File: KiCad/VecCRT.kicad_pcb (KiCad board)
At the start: 2 copper layers, 90 x 70 mm, 75 parts, among them J1 RaspiGPIO, J2 K2, J3 Conn_01x03, J4 Conn_01x06, J5 Conn_01x03, J6 Conn_01x06, J7 K2, Q1 2N7000, Q10 2N7000, Q2 2N7002, Q3 2N7002, Q4 2N7000, Q9 2N7000, U1 MCP4822, U2 4066, U3 4066, U4 TL072, U5 TL072, U6 4011, U7 40106, U8 4011

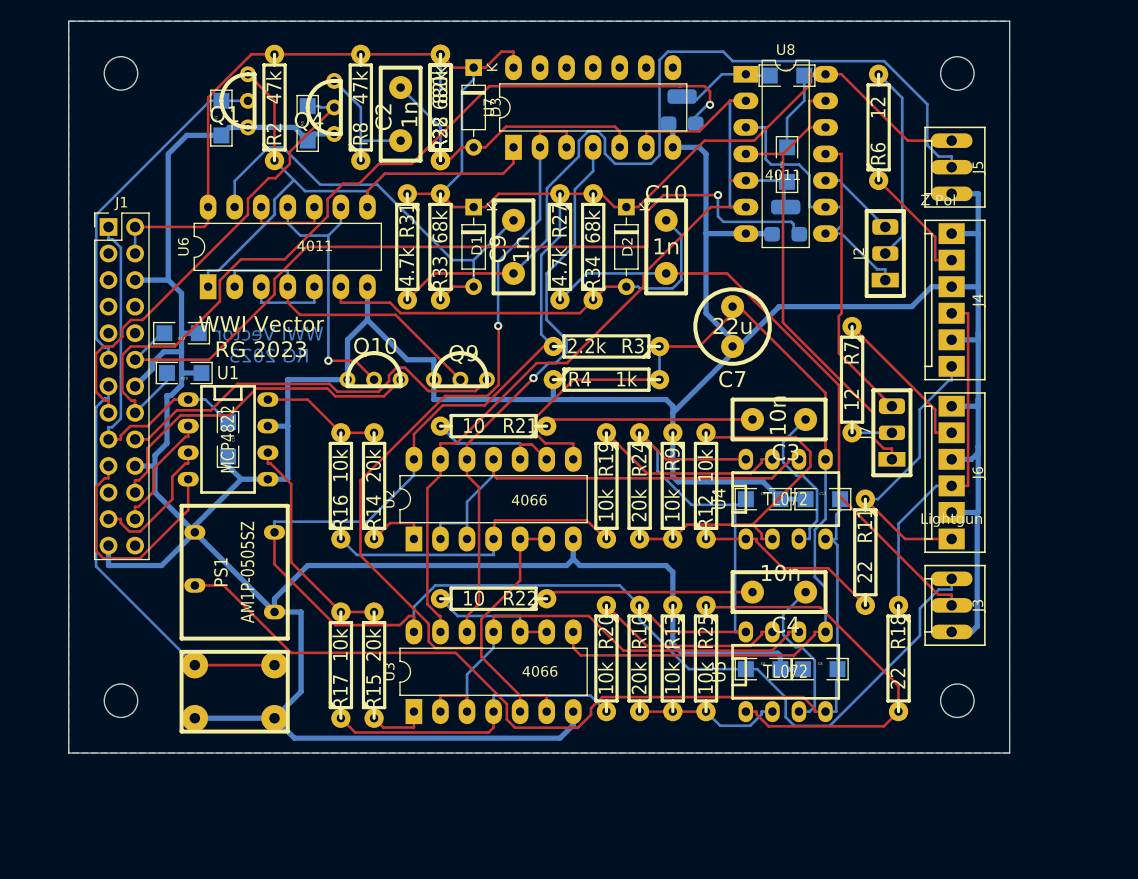
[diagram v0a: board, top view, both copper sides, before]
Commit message: new one-shot light-gun
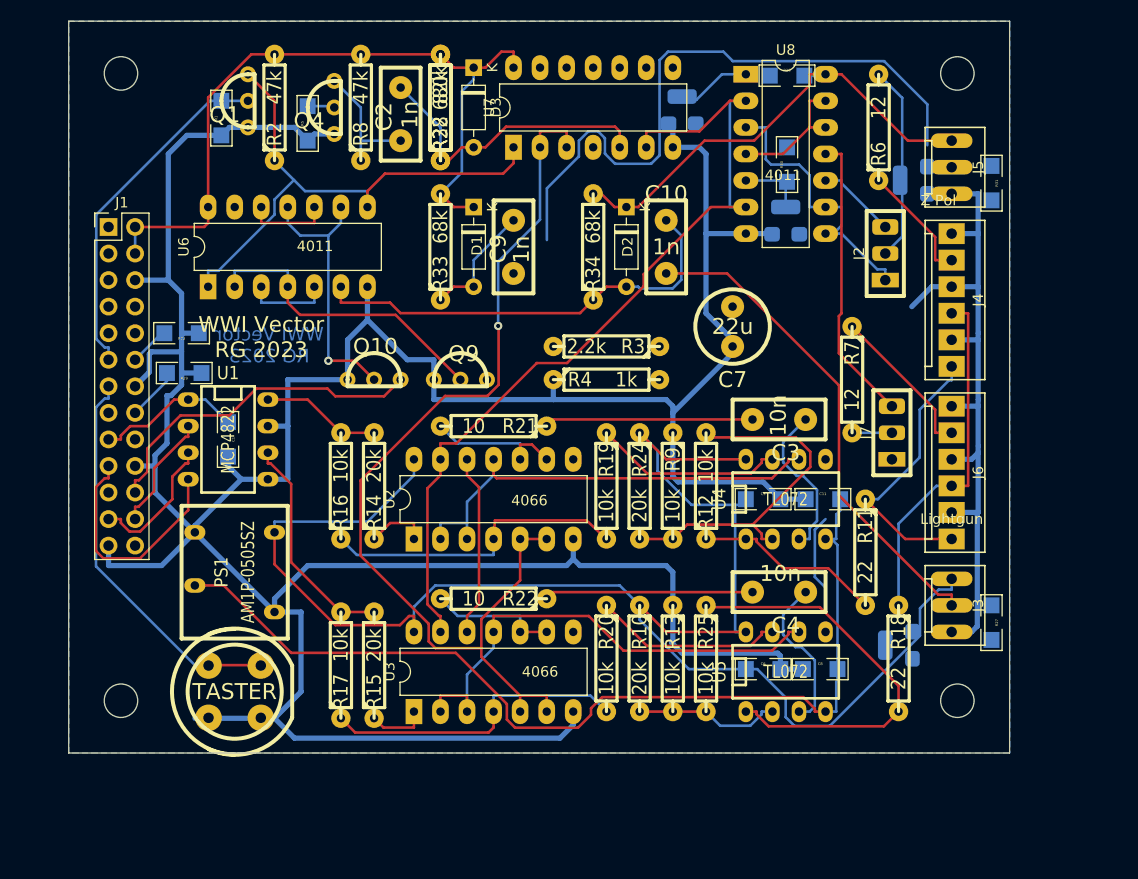
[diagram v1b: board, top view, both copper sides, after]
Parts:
- added Q5: 2N7002, RG:SOT-23_GDS, B.Cu at (80.8, 15.2)
- added Q6: 2N7002, RG:SOT-23_GDS, B.Cu at (79.4, 59.7)
- R27, R31: value 4.7k -> 470k; footprint RG:R4-2 -> RG:SM-1206B
- S1: footprint RG:Tast2mil -> RG:Tast-DT6
- moved R31 56.2 mm to (88.3, 15.5)
- moved R27 54.7 mm to (88.3, 57.5)
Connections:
- C10 pad 1: Net-(C10-Pad1) -> Net-(R27-Pad1)
- J1 pad 26: unconnected-(J1-Pad26) -> /isGun2on
- J1 pad 7: unconnected-(J1-Pad7) -> /isGun1on
- J1 pad 9: unconnected-(J1-Pad9) -> GND
- J3 pad 2: Net-(C10-Pad1) -> Net-(R27-Pad1)
- R27 pad 1: +5V -> Net-(R27-Pad1)
- R27 pad 2: Net-(C10-Pad1) -> GND
- R31 pad 1: +5V -> Net-(C9-Pad1)
- R31 pad 2: Net-(C9-Pad1) -> GND
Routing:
- net GND: track 601.6 -> 487.9 mm, vias 2 -> 0
- net /mid: track 95.4 -> 0.00 mm
- net Net-(C9-Pad1): track 81.9 -> 0.00 mm
- net +5V: track 337.7 -> 276.6 mm
- net Net-(C10-Pad1): track 58.4 -> 0.00 mm
- net Net-(R27-Pad1): track 0.00 -> 47.2 mm
- net /doDRAW: track 43.5 -> 2.59 mm
- net /isGUN2: track 38.8 -> 0.00 mm
- net /~{move}: track 54.4 -> 17.5 mm, vias 1 -> 0
- net Net-(J7-Pad3): track 46.7 -> 12.7 mm
- net Net-(C9-Pad2): track 42.8 -> 11.6 mm
- net /V_ADC: track 35.8 -> 14.1 mm
- net /~{enZ2}: track 0.00 -> 5.07 mm
- net /~{enZ1}: track 0.00 -> 3.85 mm
- net /enZ1: track 9.43 -> 7.10 mm
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
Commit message: KiCad: EDA updates for PCB production; preliminary tap and switches; ReadMe.md updated
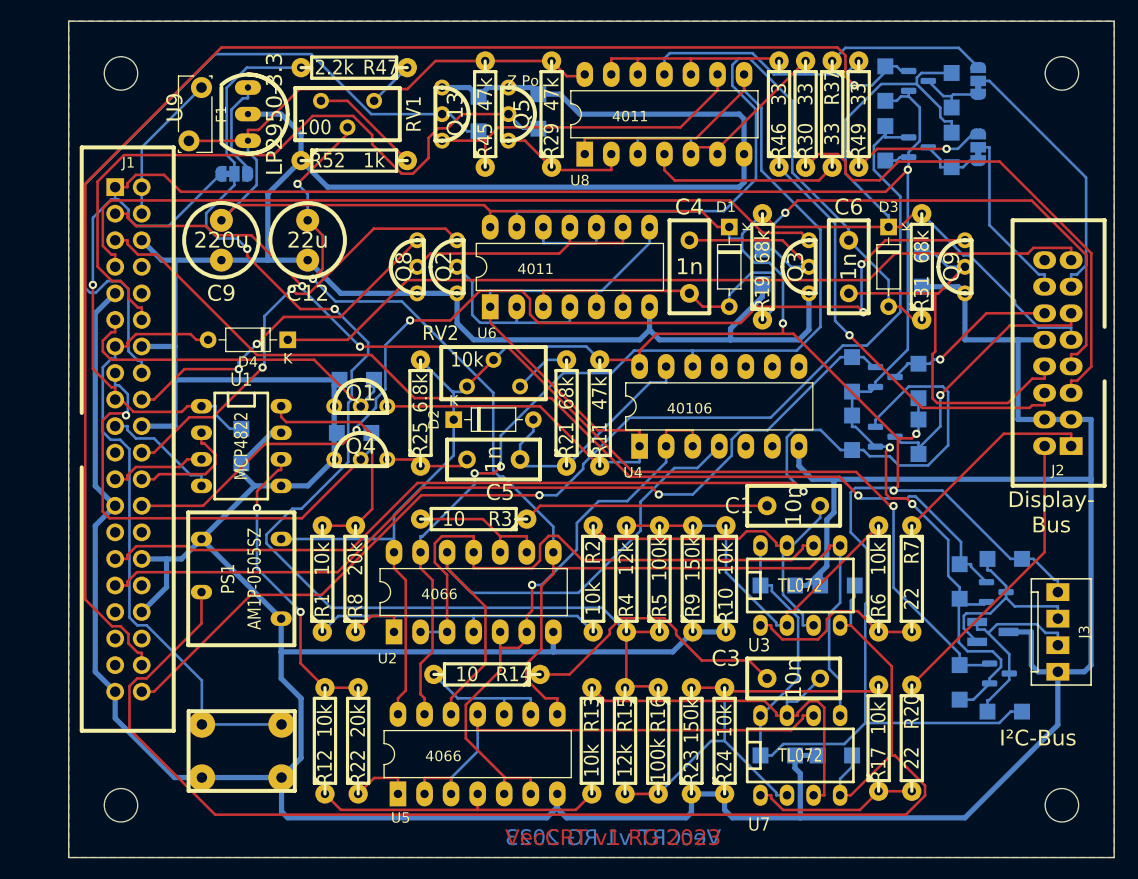
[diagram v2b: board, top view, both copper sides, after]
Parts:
- removed the C4 at (67.9, 54.6)
- removed the D1 at (38.7, 17.8)
- removed J4, J6: Conn_01x06, RG:PSS_6
- removed J5: Conn_01x03, RG:PSS_3
- removed J7: K2, RG:Pins_3
- removed the Q2 at (58.7, 8.51)
- removed the Q3 at (68.6, 19.1)
- removed the R1 at (14.6, 9.27)
- removed the R10 at (54.6, 61.0)
- removed the R2 at (19.7, 8.26)
- removed the R25 at (61.0, 61.0)
- removed R26: 47k, RG:SM-1206B
- removed the R28 at (35.6, 8.26)
- removed the R6 at (77.5, 10.2)
- removed the R7 at (74.9, 34.3)
- removed the U3 at (33.0, 66.0)
- added C3: 10n, RG:C2-2, F.Cu at (69.3, 62.9)
- added C6: 1n, RG:C2-2, F.Cu at (74.6, 23.5)
- added D3: 1N914, Diode_THT:D_DO-35_SOD27_P7.62mm_Horizontal, F.Cu at (78.4, 19.7)
- added D4: BAT41, Diode_THT:D_DO-35_SOD27_P7.62mm_Horizontal, F.Cu at (21.0, 30.5)
- added D5: ESDA5V3, Package_TO_SOT_SMD:SOT-23_Handsoldering, B.Cu at (88.4, 58.4)
- added F1: Polyfuse, Fuse:Fuse_Bourns_MF-RG300, F.Cu at (12.7, 6.35)
- added JP1: SolderJumper_3_Open, Jumper:SolderJumper-3_P1.3mm_Bridged12_RoundedPad1.0x1.5mm, B.Cu at (87.0, 5.71)
- added JP2: SolderJumper_3_Open, Jumper:SolderJumper-3_P1.3mm_Bridged12_RoundedPad1.0x1.5mm, B.Cu at (87.0, 12.1)
- added JP3: SolderJumper_3_Bridged12, Jumper:SolderJumper-3_P1.3mm_Bridged12_RoundedPad1.0x1.5mm, B.Cu at (15.8, 14.6)
- added Q11: BSS138, Package_TO_SOT_SMD:SOT-23, B.Cu at (81.3, 12.1)
- added Q12: BSS138, Package_TO_SOT_SMD:SOT-23, B.Cu at (88.7, 54.6)
- added Q13: 2N7000, RG:FETsgd_inline, F.Cu at (35.7, 8.89)
- added Q14: BSS138, Package_TO_SOT_SMD:SOT-23, B.Cu at (89.0, 62.4)
- added Q6: BSS138, Package_TO_SOT_SMD:SOT-23, B.Cu at (78.1, 39.8)
- added Q7: BSS138, Package_TO_SOT_SMD:SOT-23, B.Cu at (81.3, 5.71)
- added Q8: 2N7000, RG:FETsgd_inline, F.Cu at (33.3, 23.5)
- added Q9: 2N7000, RG:FETsgd_inline, F.Cu at (85.7, 23.5)
- added R11: 47k, RG:R4-2, F.Cu at (50.8, 37.5)
- added R12: 10k, RG:R4-2, F.Cu at (24.5, 68.8)
- added R14: 10, RG:R4-2, F.Cu at (40.0, 62.5)
- added R16: 100k, RG:R4-2, F.Cu at (56.4, 68.8)
- added R24: 10k, RG:R4-2, F.Cu at (62.7, 68.8)
- added R32: 6.8k, RG:SM-1206B, F.Cu at (74.9, 39.4)
- added R34: 6.8k, RG:SM-1206B, F.Cu at (78.1, 5.97)
- added R35: 12k, RG:SM-1206B, F.Cu at (84.5, 6.60)
- added R36: 47k, RG:SM-1206B, F.Cu at (44.9, 8.64)
- added R37: 33, RG:R4-2, F.Cu at (73.0, 8.89)
- added R38: 6.8k, RG:SM-1206B, F.Cu at (74.9, 33.8)
- added R39: 12k, RG:SM-1206B, F.Cu at (81.3, 34.4)
- added R40: 6.8k, RG:SM-1206B, F.Cu at (78.1, 11.7)
- added R41: 12k, RG:SM-1206B, F.Cu at (84.5, 12.3)
- added R42: 470k, RG:SM-1206B, F.Cu at (81.6, 23.7)
- added R43: 6.8k, RG:SM-1206B, F.Cu at (85.2, 53.6)
- added R44: 12k, RG:SM-1206B, F.Cu at (89.5, 51.4)
- added R45: 47k, RG:R4-2, F.Cu at (39.8, 8.89)
- added R46: 33, RG:R4-2, F.Cu at (67.9, 8.89)
- added R48: 47k, RG:SM-1206B, F.Cu at (39.2, 8.89)
- added R49: 33, RG:R4-2, F.Cu at (75.6, 8.89)
- added R5: 100k, RG:R4-2, F.Cu at (56.5, 53.3)
- added R50: 6.8k, RG:SM-1206B, F.Cu at (85.2, 63.2)
- added R51: 12k, RG:SM-1206B, F.Cu at (89.5, 66.0)
- added R9: 150k, RG:R4-2, F.Cu at (59.7, 53.3)
- added RV1: 100, RG:Pot64y, F.Cu at (26.7, 8.89)
- added RV2: 10k, RG:Pot64y, F.Cu at (40.6, 33.7)
- added U7: TL072, RG:DIP-8_300, F.Cu at (70.0, 70.2)
- added U9: LP2950-3.3, RG:TO-92ViGNDVo, F.Cu at (17.1, 8.89)
- C9: value 1n -> 220u; footprint RG:C2-2 -> RG:C2-7
- J1: value RaspiGPIO -> RaspiGPIO40; footprint Connector_PinHeader_2.54mm:PinHeader_2x13_P2.54mm_Vertical -> RG:Wannenstecker_2x20_V
- J2: value K2 -> Conn_02x08_Odd_Even; footprint RG:Pins_3 -> RG:Wannenstecker_2x08_V
- J3: value Conn_01x03 -> Conn_01x04_Female; footprint RG:PSS_3 -> RG:PSS_4
- Q10: value 2N7000 -> BSS138; footprint RG:FETsgd_inline -> Package_TO_SOT_SMD:SOT-23; moved to B.Cu
- Q3: renamed from Q6; value 2N7002 -> 2N7000; footprint RG:SOT-23_GDS -> RG:FETsgd_inline; moved to F.Cu
- Q5: value 2N7002 -> 2N7000; footprint RG:SOT-23_GDS -> RG:FETsgd_inline; moved to F.Cu
- R15: value 20k -> 12k
- R18: value 22 -> 47k; footprint RG:R4-2 -> RG:SM-1206B
- R20: value 10k -> 22
- R21: renamed from R32; value 680k -> 68k
- R22: value 10 -> 20k
- R23: value 47k -> 150k; footprint RG:SM-1206B -> RG:R4-2
- R25: renamed from R8; value 47k -> 6.8k
- R29: footprint RG:SM-1206B -> RG:R4-2
- R30: value 47k -> 33; footprint RG:SM-1206B -> RG:R4-2
- R31: value 470k -> 68k; footprint RG:SM-1206B -> RG:R4-2
- R33: value 68k -> 12k; footprint RG:R4-2 -> RG:SM-1206B
- R4: renamed from R24; value 20k -> 12k
- S1: footprint RG:Tast-DT6 -> RG:Tast2mil
- U4: renamed from U7; footprint Package_DIP:DIP-14_W7.62mm_LongPads -> RG:DIP-14_W7.62mm_LongPads
- U5: value TL072 -> 4066; footprint RG:DIP-8_300 -> RG:DIP-14_W7.62mm_LongPads
- moved R23 62.4 mm to (59.6, 68.8), turned to 90 degrees
- moved R18 58.3 mm to (27.6, 34.3), turned to 0 degrees
- moved R17 51.9 mm to (77.5, 68.6)
- moved R33 49.2 mm to (81.3, 39.8)
- moved Q10 48.9 mm to (78.1, 34.0), turned to 0 degrees
- moved R29 43.0 mm to (46.2, 8.89), turned to 90 degrees
- moved C12 41.5 mm to (22.9, 21.0)
- moved R27 40.5 mm to (66.4, 23.5)
- moved Q5 39.3 mm to (42.1, 8.89), turned to 0 degrees
- moved U5 38.9 mm to (31.5, 73.9), turned to 90 degrees
- moved Q3 37.2 mm to (70.8, 23.5), turned to 180 degrees
- moved R47 36.0 mm to (27.3, 4.45)
- moved C5 34.2 mm to (40.6, 41.9), turned to 0 degrees
- moved Q4 33.8 mm to (27.9, 41.9), turned to 90 degrees
- moved D2 33.7 mm to (36.8, 38.1), turned to 0 degrees
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- renumbered C3 to C1, C8 to C10, C7 to C12, C1 to C2, C10 to C4, C2 to C5, C5 to C7, C6 to C8, D2 to D1, D3 to D2, Q9 to Q2, R16 to R1, R9 to R10, R34 to R19, R19 to R2, R5 to R28, R21 to R3, R3 to R47, R4 to R52, R12 to R6, R11 to R7, R14 to R8, U4 to U3
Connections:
- C2 pad 1: /V_ADC -> +3.3V
- C4 pad 1: Net-(R27-Pad1) -> /gun1
- C5 pad 2: Net-(C2-Pad2) -> Net-(C5-Pad2)
- C9 pad 1: Net-(C9-Pad1) -> +5V
- C9 pad 2: Net-(C9-Pad2) -> GND
- D2 pad 2: Net-(C2-Pad2) -> Net-(C5-Pad2)
- J1 pad 1: /Vref_3.3V -> +3.3V
- J1 pad 13: /isKEY -> /isButton
- J1 pad 17: /V_ADC -> +3.3V
- J1 pad 2: +5V -> Net-(F1-Pad1)
- J1 pad 3: unconnected-(J1-Pad3) -> /SDA_3
- J1 pad 4: +5V -> Net-(F1-Pad1)
- J1 pad 5: unconnected-(J1-Pad5) -> /SCL_3
- J2 pad 1: Net-(J2-Pad1) -> /Xout
- J2 pad 2: Net-(J2-Pad2) -> /Yout
- J2 pad 3: Net-(J2-Pad3) -> GND
- J3 pad 2: Net-(R27-Pad1) -> Net-(D5-Pad1)
- J3 pad 3: GND -> Net-(D5-Pad2)
- Q2 pad D: /isGUN2 -> /isGUN1
- Q3 pad D: /isGun2on -> /isGun1on
- Q3 pad G: Net-(R27-Pad1) -> /gun1
- Q5 pad D: /isGun1on -> Net-(Q5-PadD)
- Q5 pad G: Net-(C9-Pad1) -> /~{enZ1}
- R13 pad 1: GND -> Net-(C3-Pad1)
- R13 pad 2: Net-(R10-Pad2) (its old number) -> Net-(R12-Pad1)
- R15 pad 1: Net-(R15-Pad1) -> /Vref_3.3V
- R15 pad 2: /Yin -> Net-(R15-Pad2)
- R17 pad 2: /Yin -> Net-(R15-Pad2)
- R18 pad 1: /Yout -> GND
- R18 pad 2: Net-(R18-Pad2) -> /doMOVE
- R20 pad 1: Net-(C4-Pad1) -> /Yout
- R21 pad 1: Net-(C2-Pad2) -> Net-(C5-Pad2)
- R21 pad 2: +5V -> Net-(R21-Pad2)
- R22 pad 1: Net-(C4-Pad2) (its old number) -> Net-(R22-Pad1)
- R22 pad 2: Net-(R22-Pad2) -> /Yin
- R23 pad 2: /~{enZ1} -> Net-(R15-Pad2)
- R27 pad 1: Net-(R27-Pad1) -> /gun1
- R29 pad 1: GND -> Net-(Q5-PadD)
- R29 pad 2: /~{enZ2} -> +5V
- R30 pad 1: /enZ2 -> /Z1
- R30 pad 2: +5V -> Net-(R30-Pad2)
- R31 pad 1: Net-(C9-Pad1) -> Net-(C6-Pad2)
- R31 pad 2: GND -> +5V
- R33 pad 1: Net-(C9-Pad2) -> /GPIO5_5
- R4 pad 1: +5V -> /Vref_3.3V
- R47 pad 1: /mid -> Net-(R47-Pad1)
- R52 pad 2: /mid -> Net-(R52-Pad2)
- S1 pad 1: GND -> /isButton
- S1 pad 2: /isKEY -> GND
- U1 pad 1: /V_ADC -> +3.3V
- U4 pad 12: (no net) -> /draw
- U4 pad 13: (no net) -> Net-(C5-Pad2)
- U4 pad 5: Net-(C2-Pad2) -> (no net)
- U4 pad 6: /draw -> (no net)
- U5 pad 1: Net-(R18-Pad2) -> Net-(R22-Pad1)
- U5 pad 2: Net-(R10-Pad2) (its old number) -> Net-(U5-Pad11)
- U5 pad 3: Net-(C4-Pad1) -> Net-(U5-Pad11)
- U5 pad 4: -5V -> Net-(R12-Pad1)
- U5 pad 5: /mid -> /move
- U5 pad 6: Net-(U3-Pad11) -> /move
- U5 pad 7: Net-(C4-Pad1) -> GND
- U5 pad 8: +5V -> /mid
- U6 pad 11: Net-(Q10-PadG) -> Net-(Q8-PadG)
- U6 pad 13: Net-(C9-Pad2) -> Net-(C6-Pad2)
- U6 pad 9: Net-(Q10-PadG) -> Net-(Q8-PadG)
- U8 pad 1: /enZ1 -> /draw
- U8 pad 10: Net-(J2-Pad1) -> Net-(R46-Pad2)
- U8 pad 12: Net-(J7-Pad3) -> Net-(R46-Pad2)
- U8 pad 13: Net-(J7-Pad3) -> Net-(R46-Pad2)
- U8 pad 2: /draw -> Net-(Q5-PadD)
- U8 pad 3: Net-(J2-Pad3) -> Net-(R30-Pad2)
- U8 pad 4: Net-(J7-Pad3) -> Net-(R37-Pad2)
- U8 pad 5: /enZ2 -> Net-(R30-Pad2)
- U8 pad 6: /draw -> Net-(R30-Pad2)
- U8 pad 8: Net-(J2-Pad3) -> /draw
- U8 pad 9: Net-(J2-Pad3) -> Net-(Q13-PadD)
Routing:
- net +3.3V: track 0.00 -> 210.5 mm, vias 0 -> 4
- net /GPIO20_3: track 0.00 -> 137.3 mm, vias 0 -> 1
- net GND: track 487.9 -> 612.1 mm
- net /mid: track 0.00 -> 121.5 mm, vias 0 -> 2
- net +5V: track 276.6 -> 396.8 mm, vias 0 -> 3
- net /Vref_3.3V: track 0.00 -> 116.4 mm, vias 0 -> 2
- net /GPIO21_3: track 0.00 -> 109.7 mm, vias 0 -> 1
- net /GPIO5_3: track 0.00 -> 107.7 mm, vias 0 -> 1
- net /SDA_3: track 0.00 -> 107.2 mm, vias 0 -> 3
- net /isGun2on: track 0.00 -> 99.2 mm, vias 0 -> 4
- net /SCL_3: track 0.00 -> 98.8 mm, vias 0 -> 1
- net /GPIO6_3: track 0.00 -> 83.8 mm, vias 0 -> 1
- net Net-(D4-Pad1): track 0.00 -> 79.7 mm
- net /isGun1on: track 0.73 -> 75.7 mm
- net Net-(C6-Pad2): track 0.00 -> 72.4 mm
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- added copper zone on B.Cu, net (none)
- added copper zone on F.Cu, net (none)
- removed copper zone on B.Cu, net GND
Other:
- board size 90 x 70 mm -> 100 x 80 mm
- board text added: "Display- Bus"
- board text added: "I²C-Bus"
- board text added: "VecCRT v1 RG 2023"
- board text removed: "Lightgun"
- board text removed: "WWI Vector RG 2023"

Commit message: Cut 3.3 / VccDAC for Arduino test
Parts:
- U4: footprint RG:DIP-14_W7.62mm_LongPads -> Package_DIP:DIP-14_W7.62mm_LongPads
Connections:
- C2 pad 1: +3.3V -> /VccDAC
- J1 pad 17: +3.3V -> /VccDAC
- U1 pad 1: +3.3V -> /VccDAC
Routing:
- net +3.3V: track 210.5 -> 174.8 mm, vias 4 -> 3
- net /VccDAC: track 0.00 -> 15.0 mm

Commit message: kicad fixes
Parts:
- added C13: 100n, RG:SM-1206B, F.Cu at (-3.81, 16.1)
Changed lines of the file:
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@@
   (net 72 "Net-(JP2-Pad3)")
   (net 73 "/GPIO20_5")
-  (net 74 "Net-(JP3-Pad3)")
+  (net 74 "Net-(C13-Pad1)")
   (net 75 "Net-(Q2-PadG)")
   (net 76 "Net-(R6-Pad1)")
@@
       (net 1 "GND") (pintype "passive"))
   )
+  (footprint "RG:SM-1206B" (layer "F.Cu")
+    (at -3.81 16.129 -90)
+    (property "Sheetfile" "VecCRT.kicad_sch")
+    (property "Sheetname" "")
+    (attr smd)
+    (fp_text reference "C13" (at 0 0) (layer "F.SilkS") hide
+      (effects (font (size 0.5 0.5) (thickness 0.1)))
+    )
+    (fp_text value "100n" (at 0 0) (layer "B.SilkS")
+      (effects (font (size 0.5 0.5) (thickness 0.1)) (justify mirror))
+    )
+    (fp_line (start 0.635 -1.016) (end 2.667 -1.016) (layer "B.SilkS") (width 0.127))
+    (fp_line (start 2.667 -1.016) (end 2.667 1.016) (layer "B.SilkS") (width 0.127))
+    (fp_line (start -0.635 -1.016) (end -2.667 -1.016) (layer "B.SilkS") (width 0.127))
+    (fp_line (start 2.667 1.016) (end 0.635 1.016) (layer "B.SilkS") (width 0.127))
+    (fp_line (start -2.667 1.016) (end -0.635 1.016) (layer "B.SilkS") (width 0.127))
+    (fp_line (start -2.667 -1.016) (end -2.667 1.016) (layer "B.SilkS") (width 0.127))
+    (pad "1" smd rect (at -1.651 0 270) (size 1.524 1.524) (layers "B.Cu" "B.Paste" "B.Mask")
+      (net 74 "Net-(C13-Pad1)") (pintype "passive"))
+    (pad "2" smd rect (at 1.651 0 270) (size 1.524 1.524) (layers "B.Cu" "B.Paste" "B.Mask")
+      (net 1 "GND") (pintype "passive"))
+    (model "smd/chip_cms.wrl"
+      (offset (xyz 0 0 0))
+      (scale (xyz 0.17 0.16 0.16))
+      (rotate (xyz 0 0 0))
+    )
+  )
   (footprint "RG:R4-2" (layer "F.Cu")
     (at 56.388 68.834 -90)
@@
       (net 8 "+5V") (pinfunction "Vi") (pintype "input"))
     (pad "Vo" thru_hole oval locked (at 2.54 0 90) (size 1.4 2.5) (drill 0.6) (layers *.Cu *.Mask "F.SilkS")
-      (net 74 "Net-(JP3-Pad3)") (pinfunction "Vo") (pintype "power_out"))
+      (net 74 "Net-(C13-Pad1)") (pinfunction "Vo") (pintype "power_out"))
   )
   (footprint "Diode_THT:D_DO-35_SOD27_P7.62mm_Horizontal" (layer "F.Cu")
@@
       (net 54 "/Vref_3.3V") (pinfunction "C") (pintype "passive"))
     (pad "3" smd custom (at 1.3 0) (size 1 0.5) (layers "B.Cu" "B.Mask")
-      (net 74 "Net-(JP3-Pad3)") (pinfunction "B") (pintype "passive") (zone_connect 2)
+      (net 74 "Net-(C13-Pad1)") (pinfunction "B") (pintype "passive") (zone_connect 2)
       (options (clearance outline) (anchor rect))
       (primitives
@@
     (connect_pads (clearance 0.508))
     (min_thickness 0.254) (filled_areas_thickness no)
-    (fill yes (thermal_gap 0.508) (thermal_bridge_width 0.508))
+    (fill (thermal_gap 0.508) (thermal_bridge_width 0.508))
     (polygon
       (pts
@@
     (connect_pads (clearance 0.508))
     (min_thickness 0.254) (filled_areas_thickness no)
-    (fill yes (thermal_gap 0.508) (thermal_bridge_width 0.508))
+    (fill (thermal_gap 0.508) (thermal_bridge_width 0.508))
     (polygon
       (pts

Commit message: Fixes in Schematics
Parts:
- added R26: 680k, RG:SM-1206B, F.Cu at (47.8, 37.8)
- D2: value 1N914 -> BAT42
- R25: value 6.8k -> 3.9k
- moved C13 25.2 mm to (19.8, 7.37)
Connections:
- J2 pad 16: unconnected-(J2-Pad16) -> -5V
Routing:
- net Net-(R21-Pad2): track 5.50 -> 9.35 mm
- net Net-(C5-Pad2): track 23.4 -> 26.5 mm
- net /draw: track 115.9 -> 119.0 mm
- net Net-(C13-Pad1): track 9.85 -> 12.8 mm
- net GND: track 612.1 -> 610.8 mm
- net -5V: track 132.9 -> 133.4 mm
